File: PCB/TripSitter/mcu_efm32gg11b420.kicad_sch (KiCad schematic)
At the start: 26 parts, among them J102 EFM32_PinHeader_PortE, J201 Conn_ARM_JTAG_SWD_20, SW1 SW_Push_Open, U201 EFM32GG11B420F2048GQ100, U202 IS62WVS2568FBLL-20NLI, Y101 48MHz

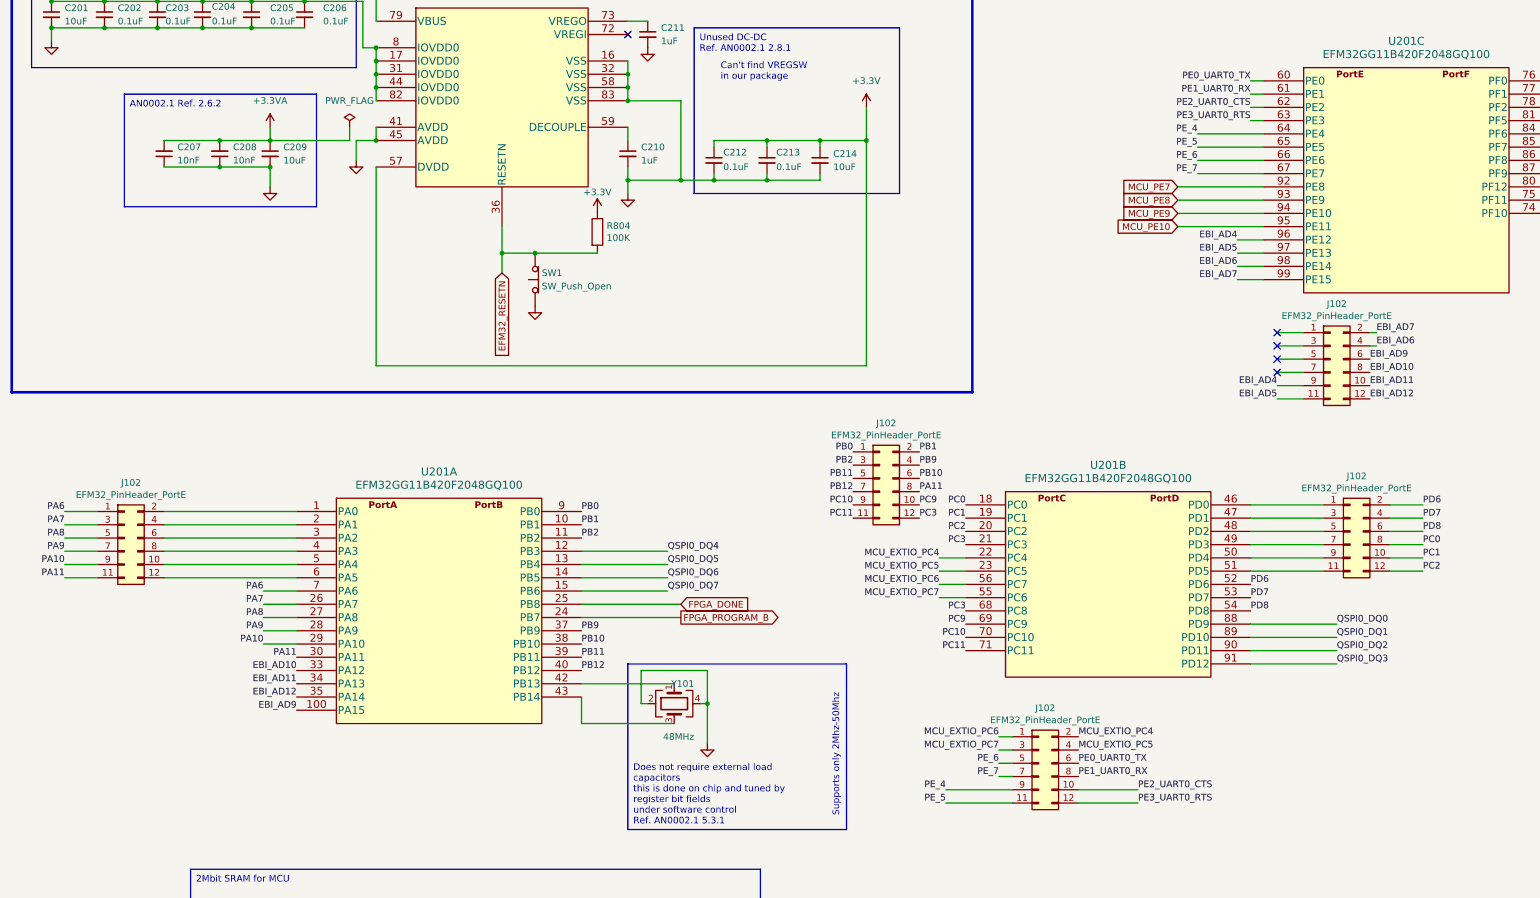
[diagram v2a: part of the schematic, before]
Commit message: pcb: Finalized routing without DDR3
Added ground and power plane, layed out all the components, fanned out
BGA. QSPI between FPGA->MCU->SRAM and MCU->SRAM is routed. Most is done
but DRC does not pass so do not produce.
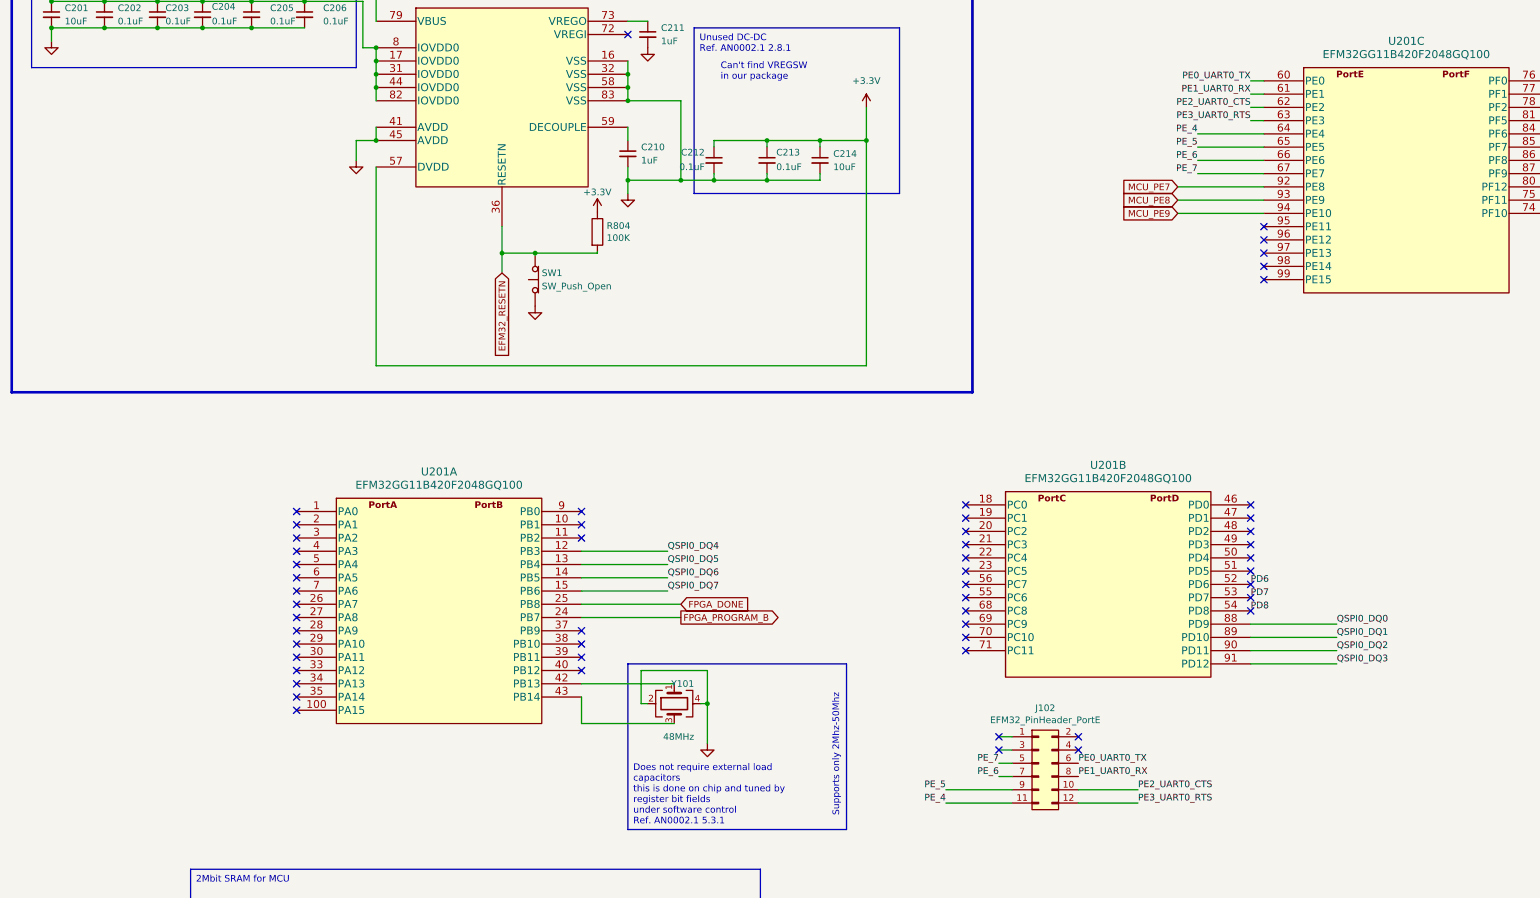
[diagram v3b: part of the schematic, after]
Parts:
- removed C207, C208: 10nF, Capacitor_SMD:C_0402_1005Metric_Pad0.74x0.62mm_HandSolder, symbol Device:C_Small
- removed C209: 10uF, Capacitor_SMD:C_0402_1005Metric_Pad0.74x0.62mm_HandSolder, symbol Device:C_Small
- removed J102 (x4): EFM32_PinHeader_PortE, Connector_PinHeader_1.00mm:PinHeader_2x06_P1.00mm_Vertical, symbol Connector_Generic:Conn_02x06_Odd_Even
- C202, C203, C204, C205, C206, C212, C213: footprint Capacitor_SMD:C_0603_1608Metric_Pad1.08x0.95mm_HandSolder -> Capacitor_SMD:C_0402_1005Metric_Pad0.74x0.62mm_HandSolder
- C210: footprint Capacitor_SMD:C_0201_0603Metric_Pad0.64x0.40mm_HandSolder -> Capacitor_SMD:C_0402_1005Metric_Pad0.74x0.62mm_HandSolder
- J201: footprint Connector_PinHeader_1.00mm:PinHeader_2x10_P1.00mm_Vertical -> Connector_PinHeader_1.27mm:PinHeader_2x10_P1.27mm_Vertical_SMD
- SW1: footprint Button_Switch_SMD:SW_Push_1P1T_NO_CK_PTS125Sx43PSMTR -> Button_Switch_SMD:SW_Push_SPST_NO_Alps_SKRK
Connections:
- net PE_4: now also J102.11 (Pin_11); no longer J102.9 (Pin_9)
- net PE_5: now also J102.9 (Pin_9); no longer J102.11 (Pin_11)
- net PE_6: now also J102.7 (Pin_7); no longer J102.5 (Pin_5)
- net PE_7: now also J102.5 (Pin_5); no longer J102.7 (Pin_7)
- net EBI_AD10: no longer names the net of U201.33 (PA12)
- net EBI_AD11: no longer names the net of U201.34 (PA13)
- net EBI_AD12: no longer names the net of U201.35 (PA14)
- net EBI_AD4: no longer names the net of U201.96 (PE12)
- net EBI_AD5: no longer names the net of U201.97 (PE13)
- net EBI_AD6: no longer names the net of U201.98 (PE14)
- net EBI_AD7: no longer names the net of U201.99 (PE15)
- net EBI_AD9: no longer names the net of U201.100 (PA15)
- net MCU_EXTIO_PC4: no longer names the net of U201.22 (PC4)
- net MCU_EXTIO_PC4: no longer J102.2 (Pin_2)
- net MCU_EXTIO_PC5: no longer names the net of U201.23 (PC5)
- net MCU_EXTIO_PC5: no longer J102.4 (Pin_4)
- net MCU_EXTIO_PC6: no longer names the net of U201.56 (PC7)
- net MCU_EXTIO_PC6: no longer J102.1 (Pin_1)
- net MCU_EXTIO_PC7: no longer names the net of U201.55 (PC6)
- net MCU_EXTIO_PC7: no longer J102.3 (Pin_3)
- net MCU_PE10: no longer names the net of U201.95 (PE11)
- net PA10: no longer names the net of U201.29 (PA10)
- net PA11: no longer names the net of U201.30 (PA11)
- net PA6: no longer names the net of U201.7 (PA6)
- net PA7: no longer names the net of U201.26 (PA7)
- net PA8: no longer names the net of U201.27 (PA8)
- net PA9: no longer names the net of U201.28 (PA9)
- net PB0: no longer names the net of U201.9 (PB0)
- net PB1: no longer names the net of U201.10 (PB1)
- net PB10: no longer names the net of U201.38 (PB10)
- net PB11: no longer names the net of U201.39 (PB11)
- net PB12: no longer names the net of U201.40 (PB12)
- net PB2: no longer names the net of U201.11 (PB2)
- net PB9: no longer names the net of U201.37 (PB9)
- net PC0: no longer names the net of U201.18 (PC0)
- net PC1: no longer names the net of U201.19 (PC1)
- net PC10: no longer names the net of U201.70 (PC10)
- net PC11: no longer names the net of U201.71 (PC11)
- net PC2: no longer names the net of U201.20 (PC2)
- net PC3: no longer names the net of U201.21 (PC3)
- net PC3: no longer U201.68 (PC8)
- net PC9: no longer names the net of U201.69 (PC9)
- no-connect marks 10 -> 59
